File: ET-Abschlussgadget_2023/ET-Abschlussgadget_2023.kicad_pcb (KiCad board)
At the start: 2 copper layers, 85 x 54 mm, 35 parts, among them J1 PB0, J2 PB1, J3 UPDI / RESET, J4 EXTCLK, J5 EXTCLK, J6 EXTCLK, SW1 ON/OFF, U1 ATtiny414-SS

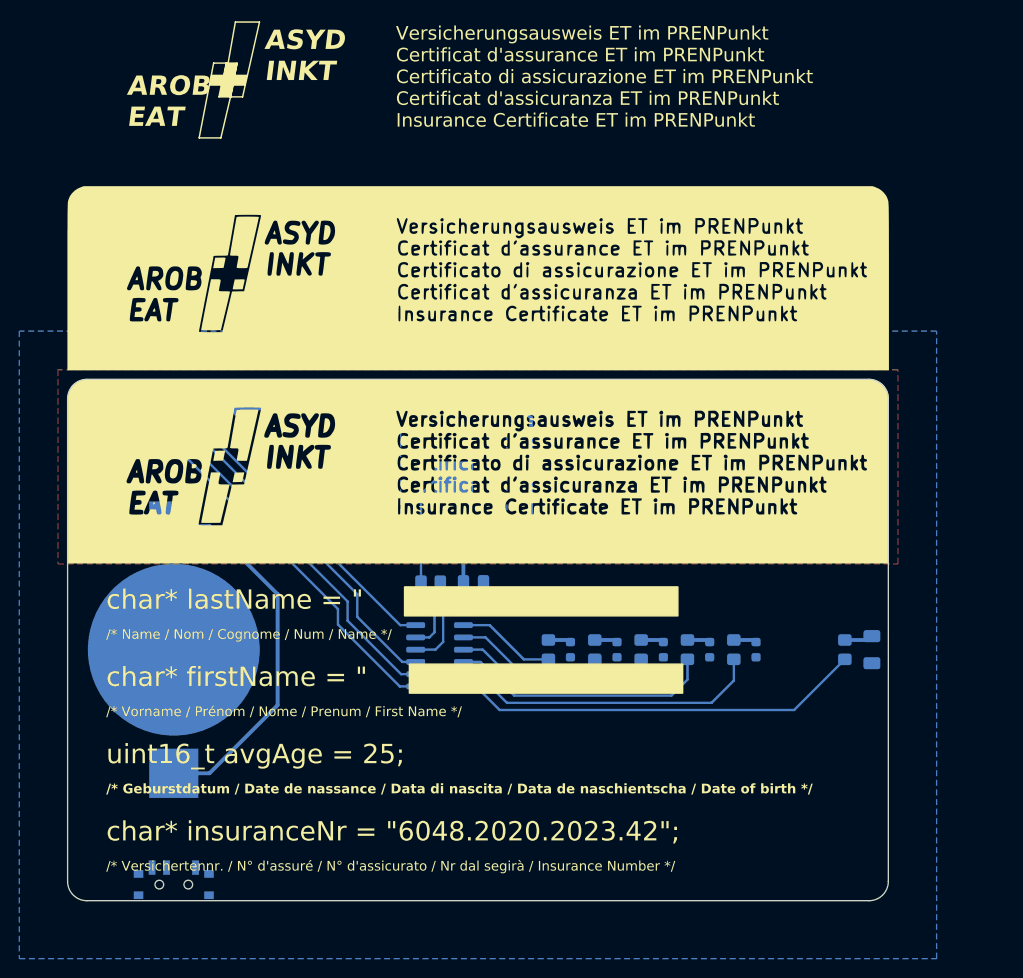
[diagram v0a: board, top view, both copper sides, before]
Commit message: Changed button-footprint, moved resistors & capacitors from 0805 to 0603, minor tweaks
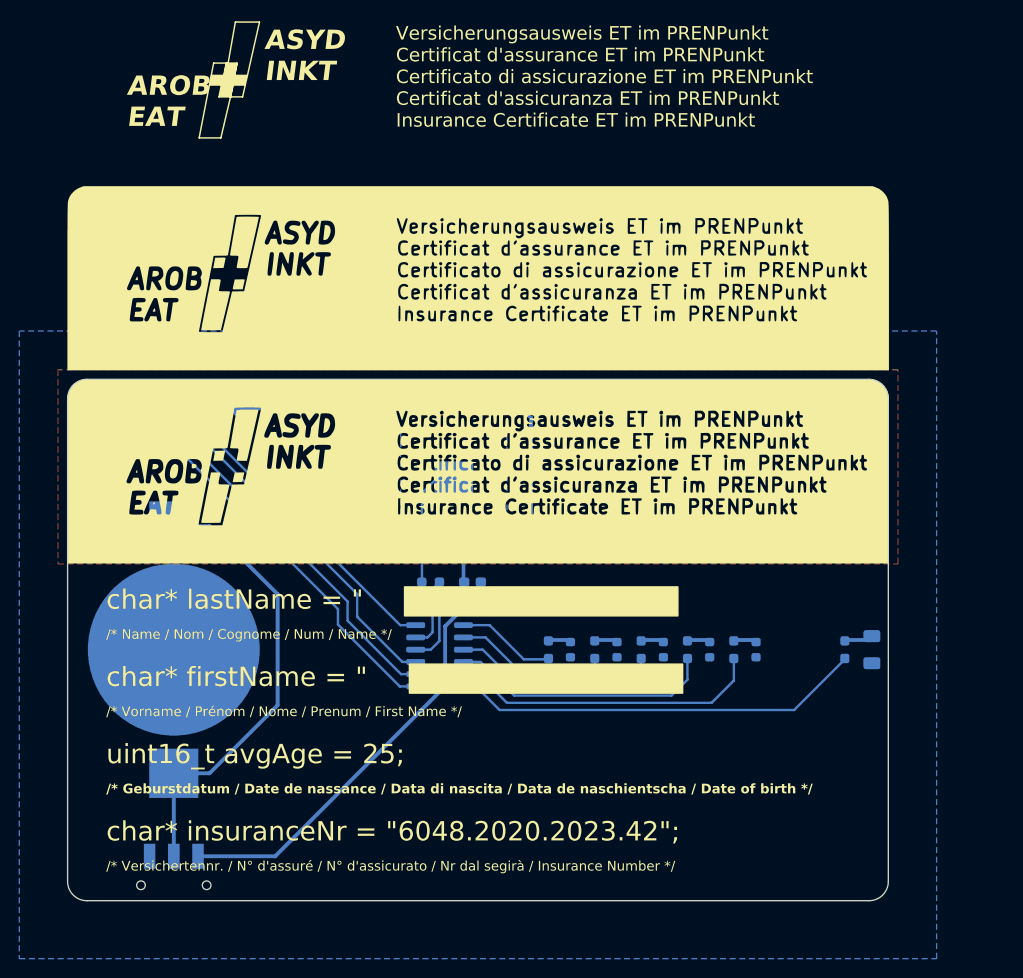
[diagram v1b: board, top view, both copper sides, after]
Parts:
- C1: footprint Capacitor_SMD:C_0805_2012Metric_Pad1.18x1.45mm_HandSolder -> Capacitor_SMD:C_0603_1608Metric_Pad1.08x0.95mm_HandSolder
- R1, R2, R3, R4, R5, R6, R7: footprint Resistor_SMD:R_0805_2012Metric_Pad1.20x1.40mm_HandSolder -> Resistor_SMD:R_0603_1608Metric_Pad0.98x0.95mm_HandSolder
- SW1: footprint Button_Switch_SMD:SW_SPDT_PCM12 -> Button_Switch_SMD:DEALON_MK-12D04-G2
- moved SW1 0.40 mm to (111.0, 132.4), turned to 0 degrees
- moved C1 0.10 mm to (141.9, 101.0)
- turned D1 to 90 degrees
- turned D2 to 90 degrees
- turned D3 to 90 degrees
- turned D4 to 90 degrees
- turned D5 to 90 degrees
- turned D6 to 90 degrees
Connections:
- D1 pad 1: Net-(D1-K) -> GND
- D1 pad 2: GND -> Net-(D1-A)
- D2 pad 1: Net-(D2-K) -> GND
- D2 pad 2: GND -> Net-(D2-A)
- D3 pad 1: Net-(D3-K) -> GND
- D3 pad 2: GND -> Net-(D3-A)
- D4 pad 1: Net-(D4-K) -> GND
- D4 pad 2: GND -> Net-(D4-A)
- D5 pad 1: Net-(D5-K) -> GND
- D5 pad 2: GND -> Net-(D5-A)
- D6 pad 1: Net-(D6-K) -> GND
- D6 pad 2: GND -> Net-(D6-A)
- R1 pad 1: Net-(D1-K) -> Net-(D1-A)
- R2 pad 1: Net-(D2-K) -> Net-(D2-A)
- R3 pad 2: Net-(D3-K) -> Net-(D3-A)
- R4 pad 2: Net-(D4-K) -> Net-(D4-A)
- R6 pad 1: Net-(D5-K) -> Net-(D5-A)
- R7 pad 1: Net-(D6-K) -> Net-(D6-A)
- SW1 pad 1: VCC -> unconnected-(SW1-A-Pad1)
- SW1 pad 3: unconnected-(SW1-C-Pad3) -> VCC
- U1 pad 12: /Cap_Pad -> /Cap_Pad / ADC1
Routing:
- net VCC: track 56.0 -> 97.5 mm
- net Net-(BT1-+): track 38.8 -> 48.0 mm
- net /Cap_Pad: track 21.0 -> 13.0 mm
- net /Cap_Pad / ADC1: track 9.51 -> 16.4 mm
- net Net-(D1-K): track 2.97 -> 0.00 mm
- net Net-(D1-A): track 0.00 -> 2.97 mm
- net Net-(D5-K): track 2.39 -> 0.00 mm
- net Net-(D5-A): track 0.00 -> 2.39 mm
- net Net-(D3-K): track 2.39 -> 0.00 mm
- net Net-(D3-A): track 0.00 -> 2.39 mm
- net Net-(D2-K): track 2.39 -> 0.00 mm
- net Net-(D2-A): track 0.00 -> 2.39 mm
- net Net-(D4-K): track 2.39 -> 0.00 mm
- net Net-(D4-A): track 0.00 -> 2.39 mm
- net Net-(D6-K): track 2.37 -> 0.00 mm
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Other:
- board text added: "ON"

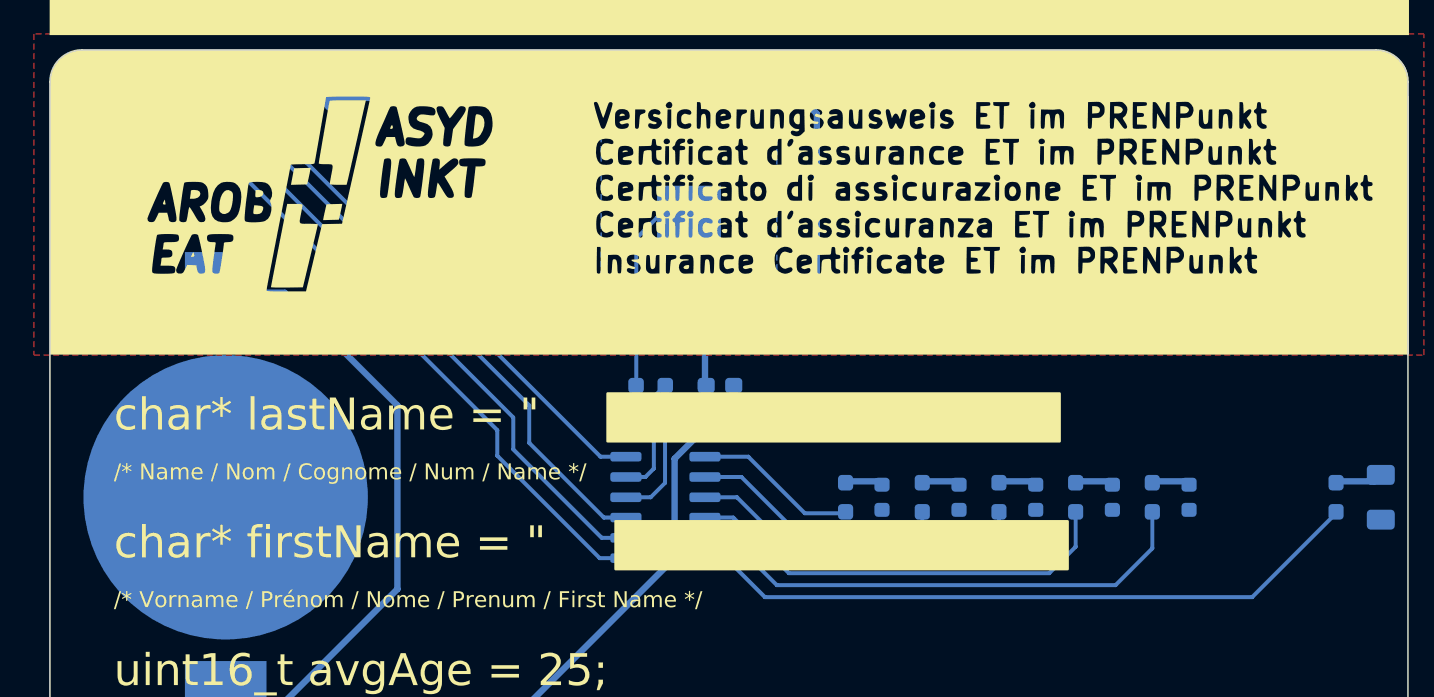
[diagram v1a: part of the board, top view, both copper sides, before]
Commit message: Improve back silkscreen and routing
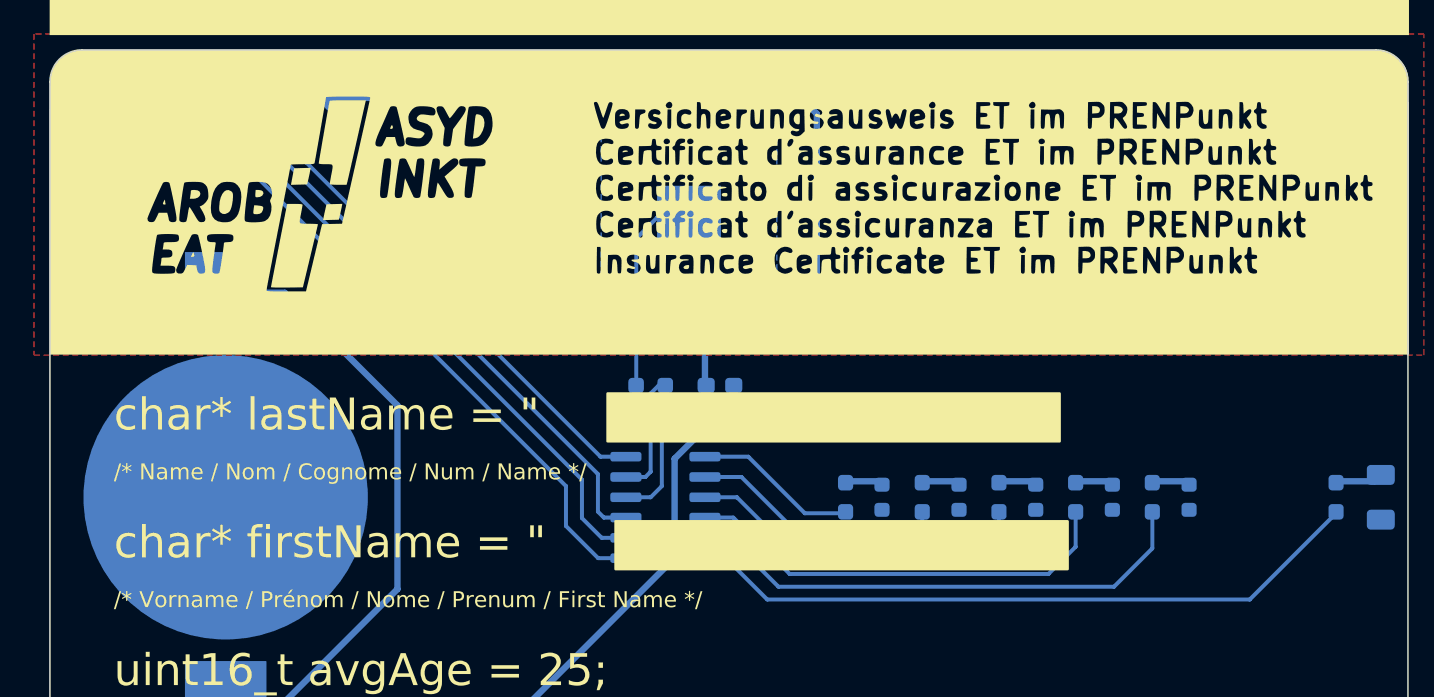
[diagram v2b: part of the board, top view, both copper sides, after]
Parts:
- added kibuzzard-64480F6A: G***, kibuzzard-64480F6A, B.Cu at (128.7, 124.8)
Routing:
- net /UPDI / RESET: track 39.3 -> 40.1 mm
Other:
- board text removed: "SCAN ME!"

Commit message: Add back copper pattern
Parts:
- G*** (x2): value LOGO -> LOGO1

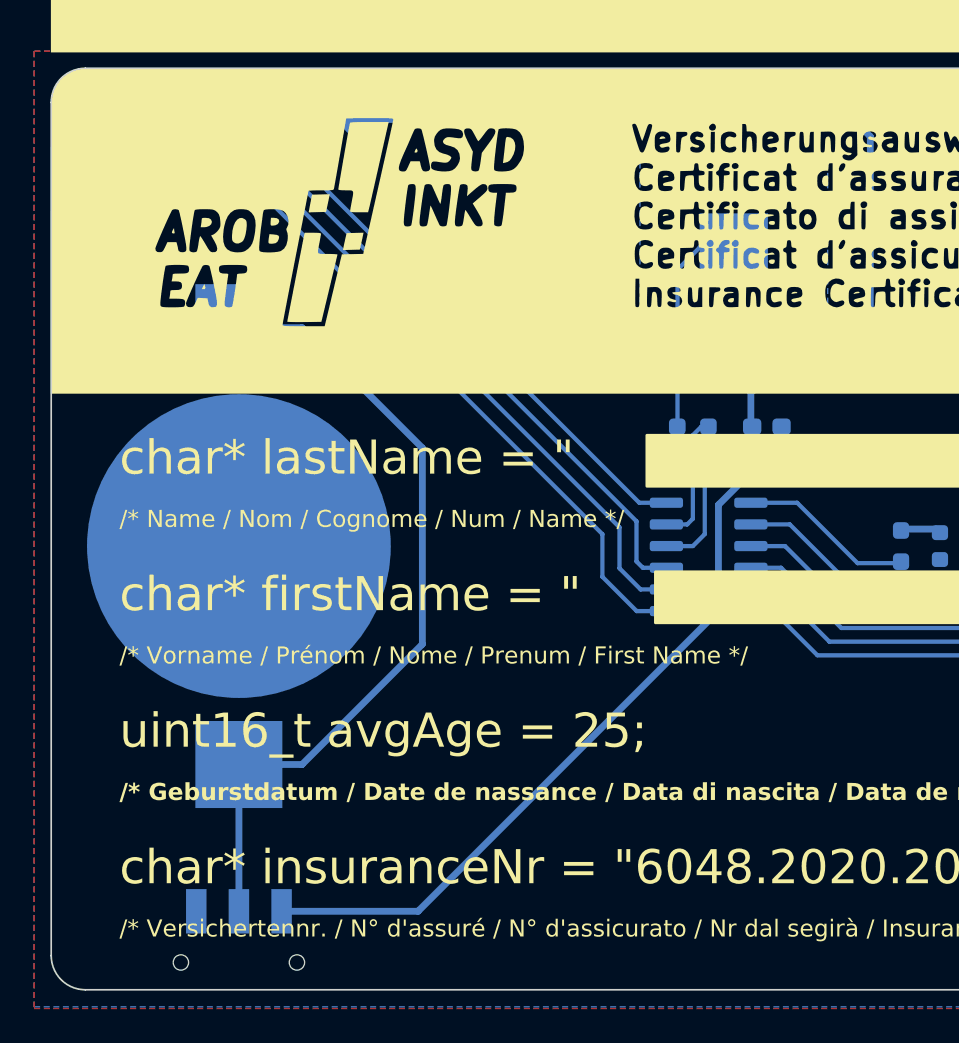
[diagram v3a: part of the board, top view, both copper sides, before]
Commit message: Updated switch & battery holder footprint, adjusted manual BOM
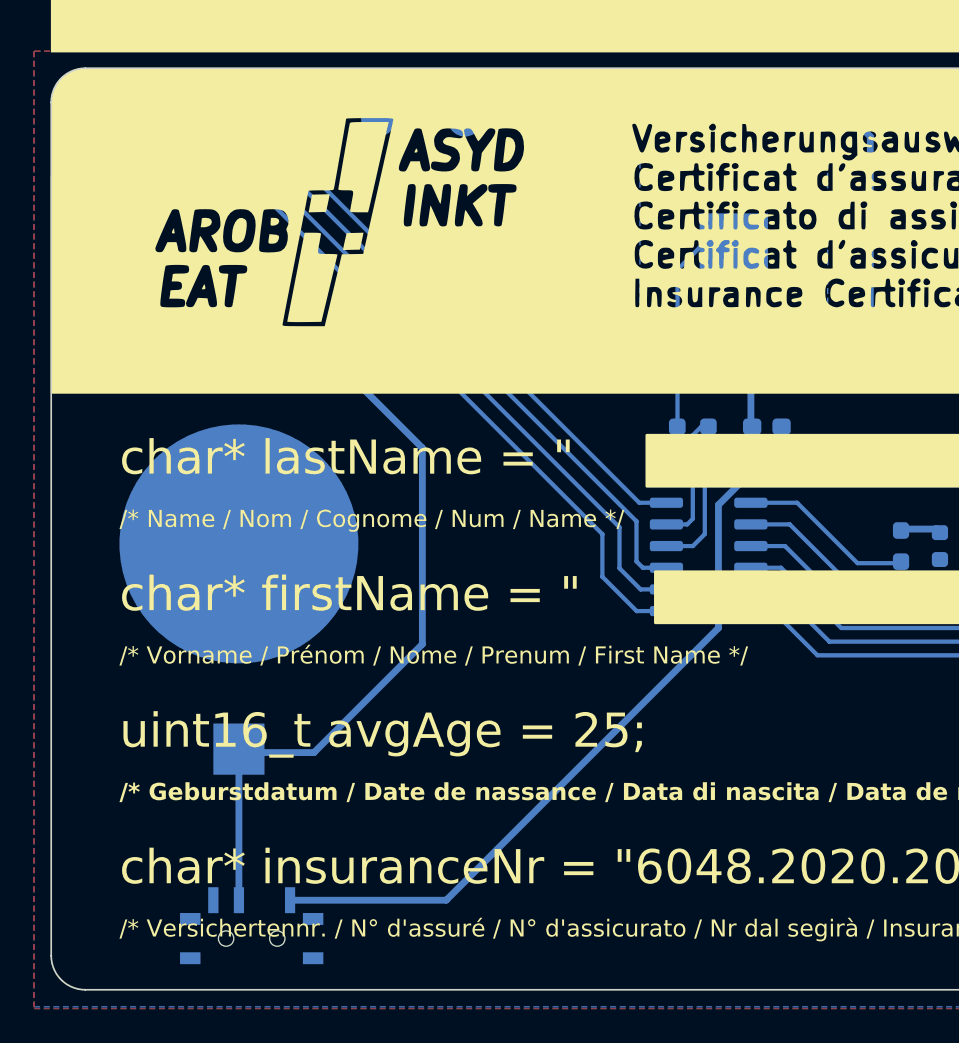
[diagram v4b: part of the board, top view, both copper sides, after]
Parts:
- BT1: footprint Battery:BatteryHolder_Keystone_3002_1x2032 -> easyeda2kicad:BAT-SMD_CR2032-3V
- SW1: footprint Button_Switch_SMD:DEALON_MK-12D04-G2 -> easyeda2kicad:SW-TH_MSK12C02
- moved J5 6.24 mm to (124.2, 83.0)
- moved J6 4.16 mm to (119.2, 83.0)
- moved SW1 2.09 mm to (111.8, 130.4), turned to 180 degrees
- moved J4 2.08 mm to (114.1, 83.0)
- moved J2 0.20 mm to (102.8, 83.0)
- turned BT1 to 180 degrees
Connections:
- SW1 pad 1: unconnected-(SW1-A-Pad1) -> VCC
- SW1 pad 3: VCC -> unconnected-(SW1-C-Pad3)
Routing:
- net VCC: track 97.5 -> 91.1 mm
- net /EXTCLK: track 33.4 -> 32.5 mm
- net Net-(BT1-+): track 48.0 -> 47.2 mm
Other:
- board text removed: "ET: {dblquote}Wie WI, nur besser{dblquote}"

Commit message: Move switch, Move testpads, Add spotify code
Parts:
- moved SW1 8.54 mm to (103.9, 127.1), turned to 90 degrees
- moved J5 7.62 mm to (116.6, 83.0)
- moved J6 5.08 mm to (114.1, 83.0)
- moved J4 2.54 mm to (111.5, 83.0)
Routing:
- net VCC: track 91.1 -> 107.4 mm
- net /EXTCLK: track 32.5 -> 34.5 mm
- net Net-(BT1-+): track 47.2 -> 48.7 mm
